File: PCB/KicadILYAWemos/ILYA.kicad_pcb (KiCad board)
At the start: 2 copper layers, 6 parts

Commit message: PCB Wemos
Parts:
- removed the REF** at (152.4, 94.0)
- removed the REF** at (158.8, 97.8)
- removed the REF** at (158.8, 87.6)
- removed the REF** at (144.8, 99.1)
- removed the REF** at (143.5, 105.4)
- removed the REF** at (143.5, 82.5)
- added REF**: PinSocket_1x08_P2.54mm_Vertical, pinSocket:PinSocket_1x08_P2.54mm_Vertical, F.Cu at (179.1, 108.0)
- added REF**: PinSocket_1x08_P2.54mm_Vertical, pinSocket:PinSocket_1x08_P2.54mm_Vertical, F.Cu at (179.1, 85.1)
- added U101: Temperature_connector, pinHeads:PinHeader_1x04_P2.54mm_Horizontal, F.Cu at (194.3, 91.4)
- added U102: WeMos_mini, wemos-d1-mini:wemos-d1-mini-with-pin-header, F.Cu at (188.0, 96.5)
- added U2: Relay_2_pins, pinHeads:PinHeader_1x02_P2.54mm_Horizontal, F.Cu at (180.3, 102.9)
- added U3101: Flow_connector, pinHeads:PinHeader_1x03_P2.54mm_Horizontal, F.Cu at (180.3, 95.2)
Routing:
- net (no net): track 109.1 -> 0.00 mm
- net GND: track 0.00 -> 40.6 mm
- net Net-(U101-Pad4): track 0.00 -> 16.1 mm
- net VCC: track 0.00 -> 15.5 mm
- net Net-(U102-Pad12): track 0.00 -> 11.0 mm
- net +5V: track 0.00 -> 5.61 mm
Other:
- board text added: "P1"

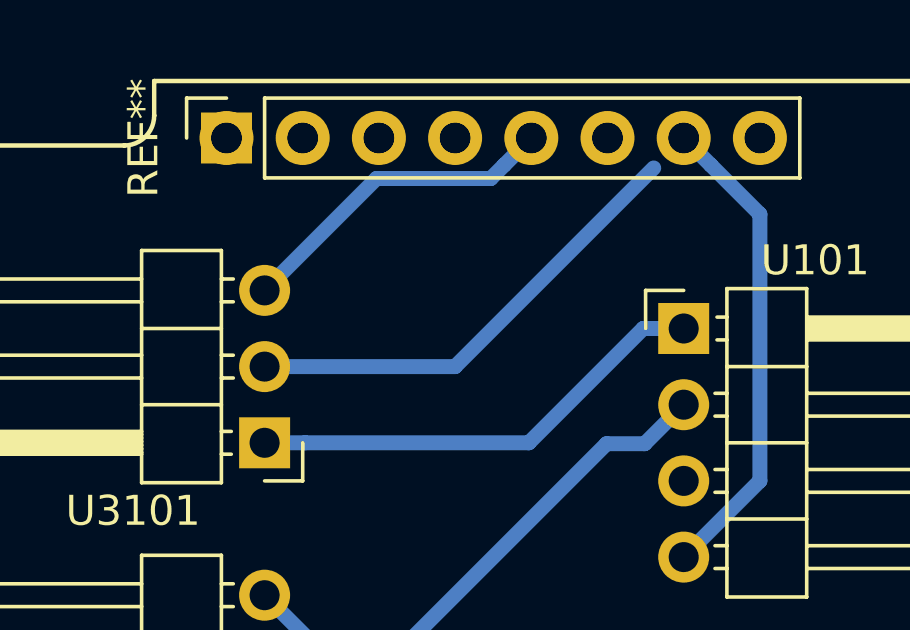
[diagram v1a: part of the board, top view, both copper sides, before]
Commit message: Wemos routage bon mais pin socket error pad near to pad
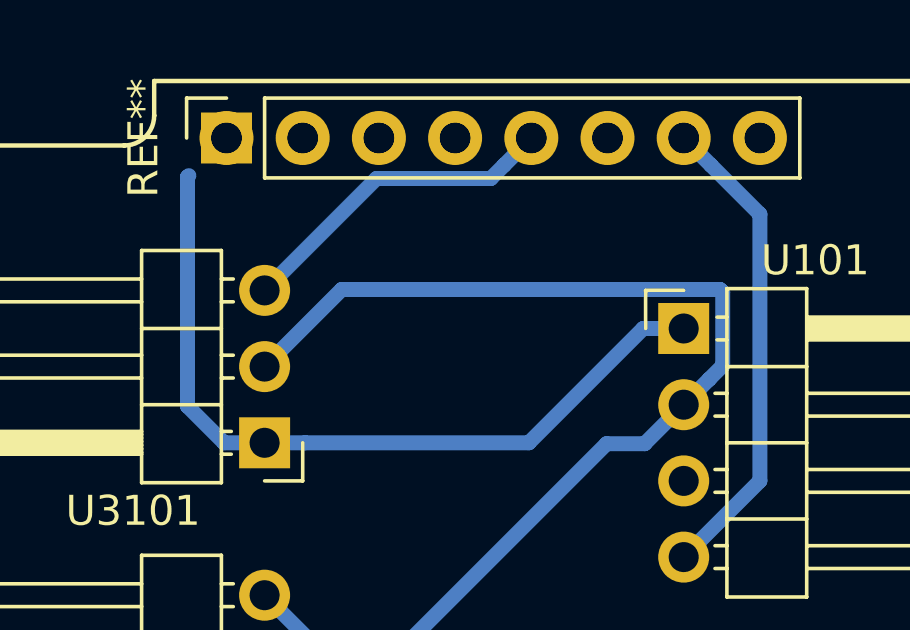
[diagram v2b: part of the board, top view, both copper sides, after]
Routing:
- net VCC: track 15.5 -> 26.3 mm
- net GND: track 40.6 -> 45.5 mm
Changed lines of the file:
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@@
     (thickness 1.6)
     (drawings 1)
-    (tracks 23)
+    (tracks 31)
     (zones 0)
     (modules 6)
@@
   (segment (start 179.07 105.49) (end 179.07 107.95) (width 0.5) (layer B.Cu) (net 1))
   (segment (start 180.34 100.33) (end 182.88 102.87) (width 0.5) (layer B.Cu) (net 2))
-  (segment (start 180.34 92.71) (end 186.69 92.71) (width 0.5) (layer B.Cu) (net 2))
-  (segment (start 186.69 92.71) (end 193.310999 86.089001) (width 0.5) (layer B.Cu) (net 2))
   (segment (start 193.009999 95.280001) (end 191.739999 95.280001) (width 0.5) (layer B.Cu) (net 2))
   (segment (start 194.31 93.98) (end 193.009999 95.280001) (width 0.5) (layer B.Cu) (net 2))
@@
   (segment (start 182.88 106.68) (end 181.61 107.95) (width 0.5) (layer B.Cu) (net 2))
   (segment (start 182.88 102.87) (end 182.88 106.68) (width 0.5) (layer B.Cu) (net 2))
+  (segment (start 195.610001 90.229999) (end 195.610001 92.679999) (width 0.5) (layer B.Cu) (net 2))
+  (segment (start 195.520001 90.139999) (end 195.610001 90.229999) (width 0.5) (layer B.Cu) (net 2))
+  (segment (start 195.159999 93.130001) (end 194.31 93.98) (width 0.5) (layer B.Cu) (net 2))
+  (segment (start 182.910001 90.139999) (end 195.520001 90.139999) (width 0.5) (layer B.Cu) (net 2))
+  (segment (start 195.610001 92.679999) (end 195.159999 93.130001) (width 0.5) (layer B.Cu) (net 2))
+  (segment (start 180.34 92.71) (end 182.910001 90.139999) (width 0.5) (layer B.Cu) (net 2))
   (segment (start 189.15 95.25) (end 181.69 95.25) (width 0.5) (layer B.Cu) (net 3))
   (segment (start 192.96 91.44) (end 189.15 95.25) (width 0.5) (layer B.Cu) (net 3))
   (segment (start 181.69 95.25) (end 180.34 95.25) (width 0.5) (layer B.Cu) (net 3))
   (segment (start 194.31 91.44) (end 192.96 91.44) (width 0.5) (layer B.Cu) (net 3))
+  (segment (start 177.769999 86.390001) (end 177.814999 86.345001) (width 0.5) (layer B.Cu) (net 3))
+  (segment (start 177.769999 94.029999) (end 177.769999 86.390001) (width 0.5) (layer B.Cu) (net 3))
+  (segment (start 178.99 95.25) (end 177.769999 94.029999) (width 0.5) (layer B.Cu) (net 3))
+  (segment (start 180.34 95.25) (end 178.99 95.25) (width 0.5) (layer B.Cu) (net 3))
   (segment (start 195.209999 85.989999) (end 194.31 85.09) (width 0.5) (layer B.Cu) (net 5))
   (segment (start 196.85 87.63) (end 195.209999 85.989999) (width 0.5) (layer B.Cu) (net 5))

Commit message: Wemos pcb good
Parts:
- removed REF** (x2): PinSocket_1x08_P2.54mm_Vertical, pinSocket:PinSocket_1x08_P2.54mm_Vertical
- added U103: Pin_socket_1x8, pinSocket:PinSocket_1x08_P2.54mm_Vertical, F.Cu at (142.2, 113.0)
- added U104: Pin-socket2_1x08, pinSocket:PinSocket_1x08_P2.54mm_Vertical2, F.Cu at (142.2, 90.2)
- U102: footprint wemos-d1-mini:wemos-d1-mini-with-pin-header -> wemos-d1-mini:wemos-d1-mini-withoutpin
- moved U101 51.8 mm to (143.5, 101.6), turned to 180 degrees
- moved U2 37.4 mm to (143.5, 109.2)
- moved U102 37.2 mm to (151.1, 101.6)
- moved U3101 23.2 mm to (157.5, 99.1), turned to 0 degrees
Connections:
- U101 pad 4: Net-(U101-Pad4) -> SIGTemp
- U3101 pad 3: Net-(U102-Pad12) -> SIGFlow
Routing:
- net SIGTemp: track 0.00 -> 23.2 mm
- net SIGFlow: track 0.00 -> 17.2 mm
- net Net-(U101-Pad4): track 16.1 -> 0.00 mm
- net Net-(U102-Pad12): track 11.0 -> 0.00 mm
- net GND: track 45.5 -> 36.1 mm
- net +5V: track 5.61 -> 4.34 mm
- net VCC: track 26.3 -> 27.6 mm
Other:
- board text removed: "P1"

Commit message: Seild Wemos good
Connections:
- net VCC renamed +3V3
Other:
- board text added: "Flow"
- board text added: "Power"
- board text added: "Sheild Wemos mini"
- board text added: "Temperature"
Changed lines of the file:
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@@
   (general
     (thickness 1.6)
-    (drawings 0)
+    (drawings 4)
     (tracks 25)
     (zones 0)
@@
   (net 1 +5V)
   (net 2 GND)
-  (net 3 VCC)
-  (net 4 "Net-(U101-Pad3)")
-  (net 5 SIGTemp)
-  (net 6 SIGFlow)
-  (net 7 "Net-(U103-Pad3)")
-  (net 8 "Net-(U103-Pad4)")
-  (net 9 "Net-(U103-Pad5)")
-  (net 10 "Net-(U103-Pad6)")
-  (net 11 "Net-(U103-Pad7)")
-  (net 12 "Net-(U103-Pad8)")
-  (net 13 "Net-(U104-Pad9)")
-  (net 14 "Net-(U104-Pad11)")
-  (net 15 "Net-(U104-Pad13)")
-  (net 16 "Net-(U104-Pad14)")
-  (net 17 "Net-(U104-Pad15)")
+  (net 3 "Net-(U101-Pad3)")
+  (net 4 SIGTemp)
+  (net 5 SIGFlow)
+  (net 6 "Net-(U103-Pad3)")
+  (net 7 "Net-(U103-Pad4)")
+  (net 8 "Net-(U103-Pad5)")
+  (net 9 "Net-(U103-Pad6)")
+  (net 10 "Net-(U103-Pad7)")
+  (net 11 "Net-(U103-Pad8)")
+  (net 12 "Net-(U104-Pad9)")
+  (net 13 "Net-(U104-Pad11)")
+  (net 14 "Net-(U104-Pad13)")
+  (net 15 "Net-(U104-Pad14)")
+  (net 16 "Net-(U104-Pad15)")
+  (net 17 +3V3)
   (net_class Default "This is the default net class."
     (clearance 0.2)
@@
     (uvia_dia 0.3)
     (uvia_drill 0.1)
+    (add_net +3V3)
     (add_net +5V)
     (add_net GND)
@@
     (add_net SIGFlow)
     (add_net SIGTemp)
-    (add_net VCC)
   )
   (module pinHeads:PinHeader_1x02_P2.54mm_Horizontal (layer F.Cu)
@@
       (effects (font (size 1 1) (thickness 0.15)))
     )
-    (fp_text value Temperature_connector (at 4.385 9.89 180) (layer F.Fab)
+    (fp_text value Temperature_connector (at 1.27 9.89 180) (layer F.Fab)
       (effects (font (size 1 1) (thickness 0.15)))
     )
@@
     )
     (pad 1 thru_hole rect (at 0 0 180) (size 1.7 1.7) (drill 1) (layers *.Cu *.Mask)
-      (net 3 VCC))
+      (net 17 +3V3))
     (pad 2 thru_hole oval (at 0 2.54 180) (size 1.7 1.7) (drill 1) (layers *.Cu *.Mask)
       (net 2 GND))
     (pad 3 thru_hole oval (at 0 5.08 180) (size 1.7 1.7) (drill 1) (layers *.Cu *.Mask)
-      (net 4 "Net-(U101-Pad3)"))
+      (net 3 "Net-(U101-Pad3)"))
     (pad 4 thru_hole oval (at 0 7.62 180) (size 1.7 1.7) (drill 1) (layers *.Cu *.Mask)
-      (net 5 SIGTemp))
+      (net 4 SIGTemp))
     (model ${KISYS3DMOD}/Connector_PinHeader_2.54mm.3dshapes/PinHeader_1x04_P2.54mm_Horizontal.wrl
       (at (xyz 0 0 0))
@@
       (effects (font (size 1 1) (thickness 0.15)))
     )
-    (fp_text value WeMos_mini (at 0 0) (layer F.Fab)
+    (fp_text value WeMos_mini (at 0 0) (layer F.Fab) hide
       (effects (font (size 1 1) (thickness 0.15)))
     )
@@
       (effects (font (size 1 1) (thickness 0.15)))
     )
-    (fp_text value Pin_socket_1x8 (at 0 20.55 90) (layer F.Fab)
+    (fp_text value Pin_socket_1x8 (at 2.54 13.97 180) (layer F.Fab)
       (effects (font (size 1 1) (thickness 0.15)))
     )
@@
       (net 2 GND))
     (pad 3 thru_hole oval (at 0 5.08 90) (size 1.7 1.7) (drill 1) (layers *.Cu *.Mask)
-      (net 7 "Net-(U103-Pad3)"))
+      (net 6 "Net-(U103-Pad3)"))
     (pad 4 thru_hole oval (at 0 7.62 90) (size 1.7 1.7) (drill 1) (layers *.Cu *.Mask)
-      (net 8 "Net-(U103-Pad4)"))
+      (net 7 "Net-(U103-Pad4)"))
     (pad 5 thru_hole oval (at 0 10.16 90) (size 1.7 1.7) (drill 1) (layers *.Cu *.Mask)
-      (net 9 "Net-(U103-Pad5)"))
+      (net 8 "Net-(U103-Pad5)"))
     (pad 6 thru_hole oval (at 0 12.7 90) (size 1.7 1.7) (drill 1) (layers *.Cu *.Mask)
-      (net 10 "Net-(U103-Pad6)"))
+      (net 9 "Net-(U103-Pad6)"))
     (pad 7 thru_hole oval (at 0 15.24 90) (size 1.7 1.7) (drill 1) (layers *.Cu *.Mask)
-      (net 11 "Net-(U103-Pad7)"))
+      (net 10 "Net-(U103-Pad7)"))
     (pad 8 thru_hole oval (at 0 17.78 90) (size 1.7 1.7) (drill 1) (layers *.Cu *.Mask)
-      (net 12 "Net-(U103-Pad8)"))
+      (net 11 "Net-(U103-Pad8)"))
     (model ${KISYS3DMOD}/Connector_PinSocket_2.54mm.3dshapes/PinSocket_1x08_P2.54mm_Vertical.wrl
       (at (xyz 0 0 0))
@@
       (effects (font (size 1 1) (thickness 0.15)))
     )
-    (fp_text value Pin-socket2_1x08 (at 0 20.55 90) (layer F.Fab)
+    (fp_text value Pin-socket2_1x08 (at -2.54 15.24 180) (layer F.Fab)
       (effects (font (size 1 1) (thickness 0.15)))
     )
@@
     (fp_line (start -1.27 -1.27) (end 0.635 -1.27) (layer F.Fab) (width 0.1))
     (pad 9 thru_hole oval (at 0 17.78 90) (size 1.7 1.7) (drill 1) (layers *.Cu *.Mask)
-      (net 13 "Net-(U104-Pad9)"))
+      (net 12 "Net-(U104-Pad9)"))
     (pad 10 thru_hole oval (at 0 15.24 90) (size 1.7 1.7) (drill 1) (layers *.Cu *.Mask)
-      (net 5 SIGTemp))
+      (net 4 SIGTemp))
     (pad 11 thru_hole oval (at 0 12.7 90) (size 1.7 1.7) (drill 1) (layers *.Cu *.Mask)
-      (net 14 "Net-(U104-Pad11)"))
+      (net 13 "Net-(U104-Pad11)"))
     (pad 12 thru_hole oval (at 0 10.16 90) (size 1.7 1.7) (drill 1) (layers *.Cu *.Mask)
-      (net 6 SIGFlow))
+      (net 5 SIGFlow))
     (pad 13 thru_hole oval (at 0 7.62 90) (size 1.7 1.7) (drill 1) (layers *.Cu *.Mask)
-      (net 15 "Net-(U104-Pad13)"))
+      (net 14 "Net-(U104-Pad13)"))
     (pad 14 thru_hole oval (at 0 5.08 90) (size 1.7 1.7) (drill 1) (layers *.Cu *.Mask)
-      (net 16 "Net-(U104-Pad14)"))
+      (net 15 "Net-(U104-Pad14)"))
     (pad 15 thru_hole oval (at 0 2.54 90) (size 1.7 1.7) (drill 1) (layers *.Cu *.Mask)
-      (net 17 "Net-(U104-Pad15)"))
+      (net 16 "Net-(U104-Pad15)"))
     (pad 16 thru_hole rect (at 0 0 90) (size 1.7 1.7) (drill 1) (layers *.Cu *.Mask)
-      (net 3 VCC))
+      (net 17 +3V3))
     (model ${KISYS3DMOD}/Connector_PinSocket_2.54mm.3dshapes/PinSocket_1x08_P2.54mm_Vertical.wrl
       (at (xyz 0 0 0))
@@
     )
     (fp_text value Flow_connector (at 4.385 7.35) (layer F.Fab)
-      (effects (font (size 1 1) (thickness 0.15)))
+      (effects (font (size 1 1) (thickness 0.15) italic))
     )
     (fp_line (start 2.135 -1.27) (end 4.04 -1.27) (layer F.Fab) (width 0.1))
@@
     )
     (pad 1 thru_hole rect (at 0 0) (size 1.7 1.7) (drill 1) (layers *.Cu *.Mask)
-      (net 3 VCC))
+      (net 17 +3V3))
     (pad 2 thru_hole oval (at 0 2.54) (size 1.7 1.7) (drill 1) (layers *.Cu *.Mask)
       (net 2 GND))
     (pad 3 thru_hole oval (at 0 5.08) (size 1.7 1.7) (drill 1) (layers *.Cu *.Mask)
-      (net 6 SIGFlow))
+      (net 5 SIGFlow))
     (model ${KISYS3DMOD}/Connector_PinHeader_2.54mm.3dshapes/PinHeader_1x03_P2.54mm_Horizontal.wrl
       (at (xyz 0 0 0))
@@
       (rotate (xyz 0 0 0))
     )
+  )
+  (gr_text Flow (at 152.4 102.87) (layer F.Cu)
+    (effects (font (size 1.5 1.5) (thickness 0.3)))
+  )
+  (gr_text Temperature (at 152.4 96.52) (layer F.Cu)
+    (effects (font (size 1.5 1.5) (thickness 0.3)))
+  )
+  (gr_text Power (at 148.59 107.95) (layer F.Cu)
+    (effects (font (size 1.5 1.5) (thickness 0.3)))
+  )
+  (gr_text "Sheild Wemos mini" (at 156.21 93.98) (layer F.Cu)
+    (effects (font (size 1.5 1.5) (thickness 0.3)))
   )
   (segment (start 143.51 111.76) (end 142.24 113.03) (width 0.5) (layer F.Cu) (net 1))
@@
   (segment (start 142.209999 100.360001) (end 142.209999 104.14) (width 0.5) (layer B.Cu) (net 2))
   (segment (start 142.209999 104.14) (end 142.209999 110.459999) (width 0.5) (layer B.Cu) (net 2))
-  (segment (start 151.13 99.06) (end 142.24 90.17) (width 0.5) (layer B.Cu) (net 3))
-  (segment (start 157.48 99.06) (end 151.13 99.06) (width 0.5) (layer B.Cu) (net 3))
-  (segment (start 147.4 99.06) (end 151.13 99.06) (width 0.5) (layer B.Cu) (net 3))
-  (segment (start 144.86 101.6) (end 147.4 99.06) (width 0.5) (layer B.Cu) (net 3))
-  (segment (start 143.51 101.6) (end 144.86 101.6) (width 0.5) (layer B.Cu) (net 3))
-  (segment (start 156.630001 89.320001) (end 157.48 90.17) (width 0.5) (layer B.Cu) (net 5))
-  (segment (start 156.179999 88.869999) (end 156.630001 89.320001) (width 0.5) (layer B.Cu) (net 5))
-  (segment (start 140.939999 91.409999) (end 140.939999 88.959999) (width 0.5) (layer B.Cu) (net 5))
-  (segment (start 141.029999 88.869999) (end 156.179999 88.869999) (width 0.5) (layer B.Cu) (net 5))
-  (segment (start 140.939999 88.959999) (end 141.029999 88.869999) (width 0.5) (layer B.Cu) (net 5))
-  (segment (start 143.51 93.98) (end 140.939999 91.409999) (width 0.5) (layer B.Cu) (net 5))
-  (segment (start 153.249999 91.019999) (end 152.4 90.17) (width 0.5) (layer B.Cu) (net 6))
-  (segment (start 158.780001 96.550001) (end 153.249999 91.019999) (width 0.5) (layer B.Cu) (net 6))
-  (segment (start 158.780001 102.839999) (end 158.780001 96.550001) (width 0.5) (layer B.Cu) (net 6))
-  (segment (start 157.48 104.14) (end 158.780001 102.839999) (width 0.5) (layer B.Cu) (net 6))
+  (segment (start 156.630001 89.320001) (end 157.48 90.17) (width 0.5) (layer B.Cu) (net 4))
+  (segment (start 156.179999 88.869999) (end 156.630001 89.320001) (width 0.5) (layer B.Cu) (net 4))
+  (segment (start 140.939999 91.409999) (end 140.939999 88.959999) (width 0.5) (layer B.Cu) (net 4))
+  (segment (start 141.029999 88.869999) (end 156.179999 88.869999) (width 0.5) (layer B.Cu) (net 4))
+  (segment (start 140.939999 88.959999) (end 141.029999 88.869999) (width 0.5) (layer B.Cu) (net 4))
+  (segment (start 143.51 93.98) (end 140.939999 91.409999) (width 0.5) (layer B.Cu) (net 4))
+  (segment (start 153.249999 91.019999) (end 152.4 90.17) (width 0.5) (layer B.Cu) (net 5))
+  (segment (start 158.780001 96.550001) (end 153.249999 91.019999) (width 0.5) (layer B.Cu) (net 5))
+  (segment (start 158.780001 102.839999) (end 158.780001 96.550001) (width 0.5) (layer B.Cu) (net 5))
+  (segment (start 157.48 104.14) (end 158.780001 102.839999) (width 0.5) (layer B.Cu) (net 5))
+  (segment (start 151.13 99.06) (end 142.24 90.17) (width 0.5) (layer B.Cu) (net 17))
+  (segment (start 157.48 99.06) (end 151.13 99.06) (width 0.5) (layer B.Cu) (net 17))
+  (segment (start 147.4 99.06) (end 151.13 99.06) (width 0.5) (layer B.Cu) (net 17))
+  (segment (start 144.86 101.6) (end 147.4 99.06) (width 0.5) (layer B.Cu) (net 17))
+  (segment (start 143.51 101.6) (end 144.86 101.6) (width 0.5) (layer B.Cu) (net 17))
 )
